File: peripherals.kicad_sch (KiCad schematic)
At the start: 21 parts, among them U1 MIMX8MM6DVTLZAA

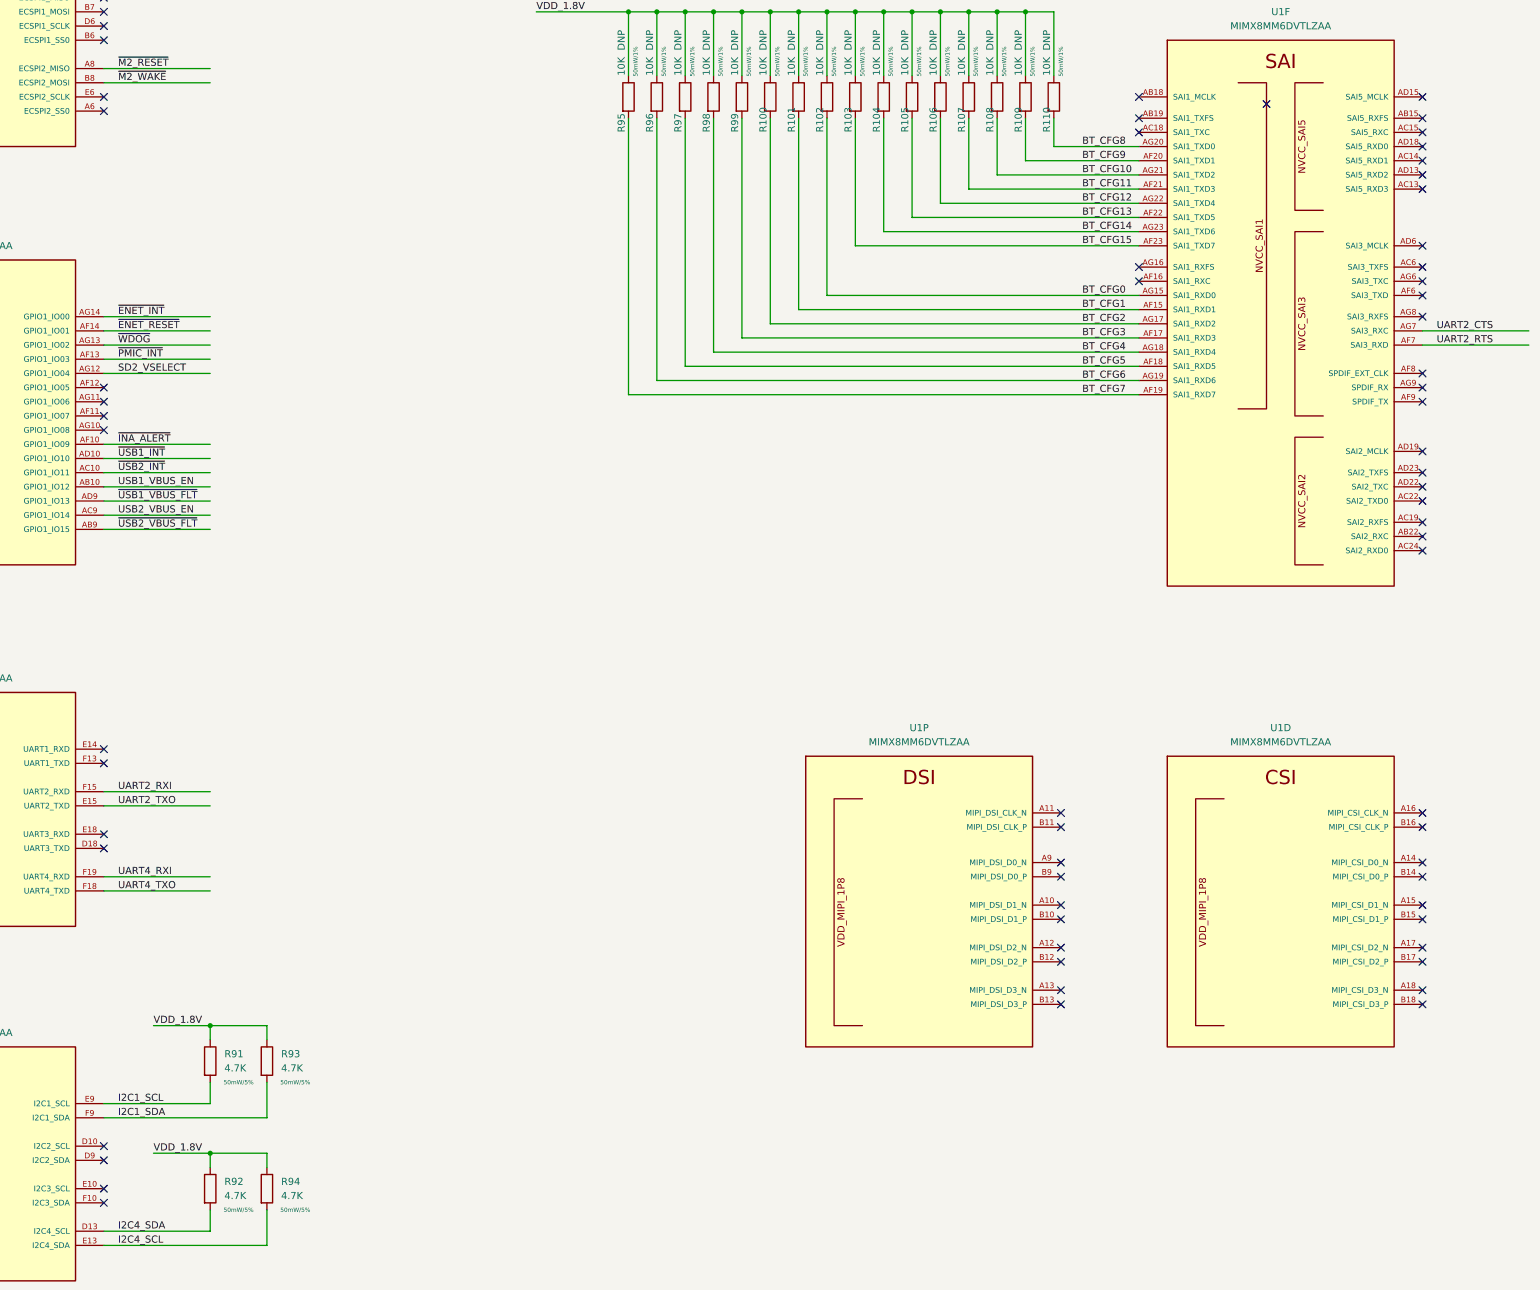
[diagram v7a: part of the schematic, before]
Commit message: add inital ddr tool version, lots of routing work
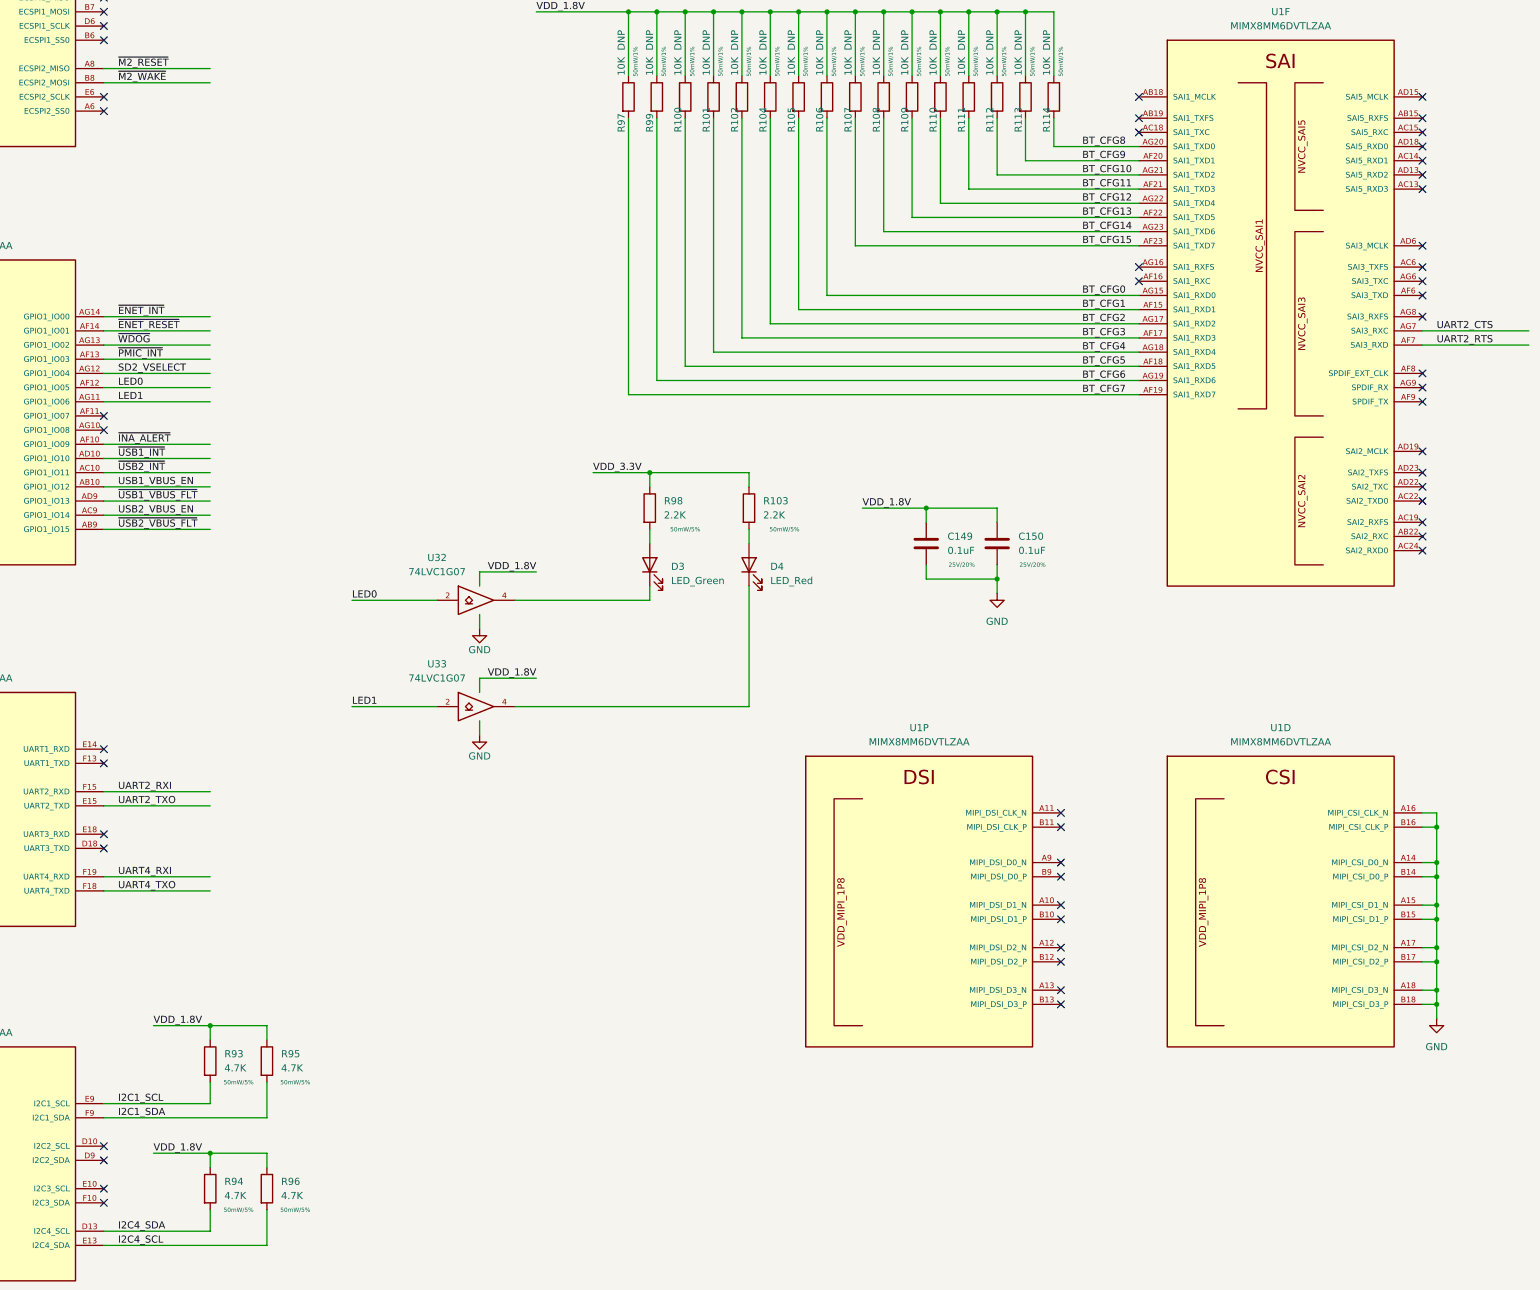
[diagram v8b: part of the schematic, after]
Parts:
- added C149, C150: 0.1uF, Capacitor_SMD:C_0402_1005Metric, symbol Device:C
- added D3: LED_Green, LED_SMD:LED_0603_1608Metric, symbol Device:LED
- added D4: LED_Red, LED_SMD:LED_0603_1608Metric, symbol Device:LED
- added R103, R98: 2.2K, Resistor_SMD:R_0402_1005Metric, symbol Device:R
- added U32, U33: 74LVC1G07, Package_TO_SOT_SMD:SOT-23-5, symbol 74xGxx:74LVC1G07
- renumbered R97 to R100, R98 to R101, R99 to R102, R100 to R104, R101 to R105, R102 to R106, R103 to R107, R104 to R108, R105 to R109, R106 to R110, R107 to R111, R108 to R112, R109 to R113, R110 to R114, R91 to R93, R92 to R94, R93 to R95, R94 to R96, R95 to R97, R96 to R99
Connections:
- net GND: now reaches U1.A14 (MIPI_CSI_D0_N)
- net GND: now also U1.A15 (MIPI_CSI_D1_N), U1.A16 (MIPI_CSI_CLK_N), U1.A17 (MIPI_CSI_D2_N), U1.A18 (MIPI_CSI_D3_N), U1.B14 (MIPI_CSI_D0_P), U1.B15 (MIPI_CSI_D1_P), U1.B16 (MIPI_CSI_CLK_P), U1.B17 (MIPI_CSI_D2_P), U1.B18 (MIPI_CSI_D3_P), C149.2, C150.2, U32.3 (GND), U33.3 (GND)
- net LED0: now reaches U1.AF12 (GPIO1_IO05)
- net LED0: now also U32.2
- net LED1: now reaches U1.AG11 (GPIO1_IO06)
- net LED1: now also U33.2
- net VDD_1.8V renamed VCC
- net VCC: now also C149.1, C150.1, U32.5 (VCC), U33.5 (VCC)
- new net: D3.2 (A), R98.2
- new net: D4.1 (K), U33.4
- new net: D3.1 (K), U32.4
- new net: D4.2 (A), R103.2
- new net VDD_3.3V: R103.1, R98.1
- no-connect marks 66 -> 53
